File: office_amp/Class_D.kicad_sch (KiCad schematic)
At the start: 40 parts, among them J3 Conn_01x02_Female, J4 Conn_01x02_Female, J5 Conn_01x02_Female, J6 Conn_01x02_Female, J7 Screw_Terminal_01x04, U6 TPA3123D2

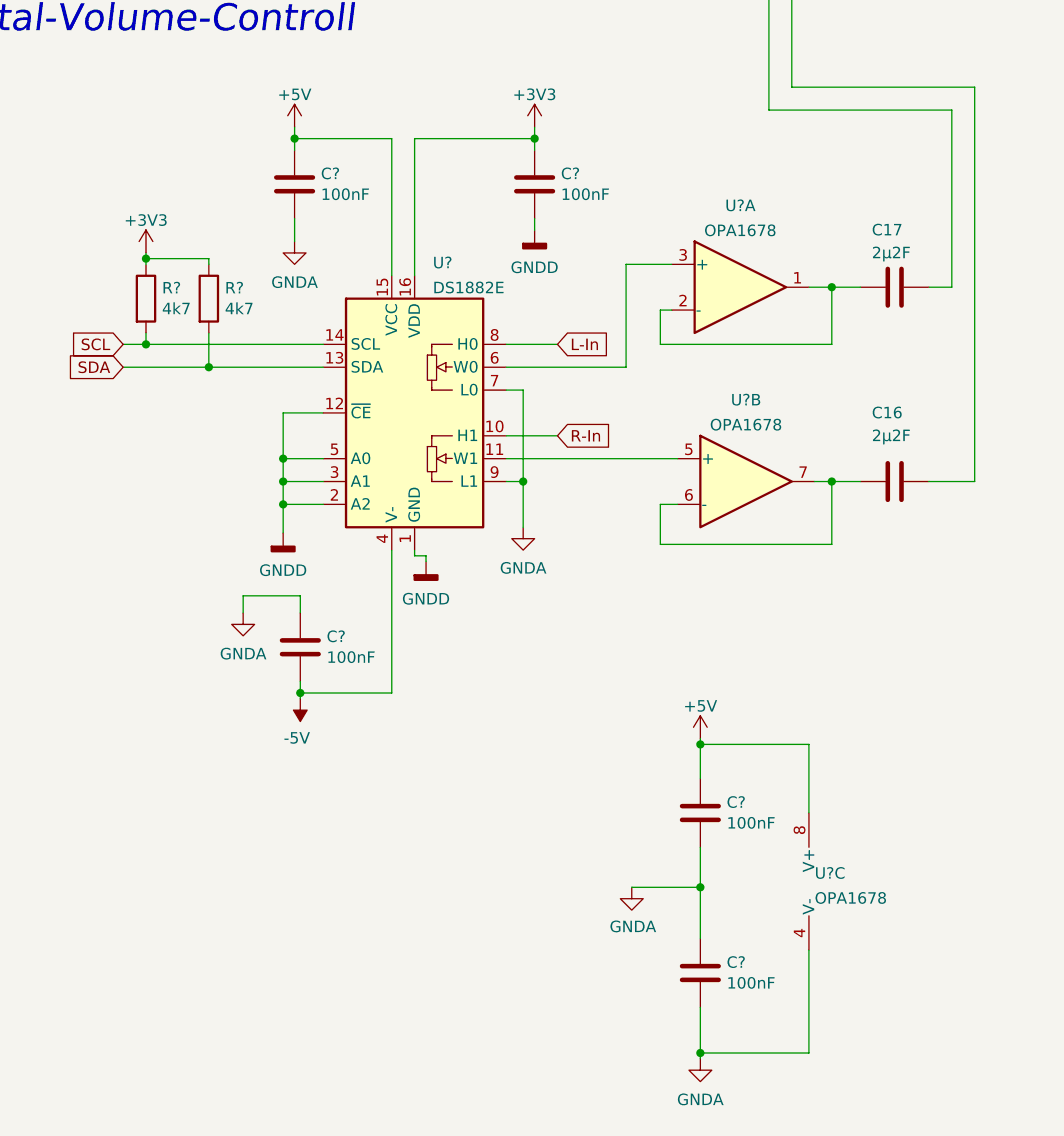
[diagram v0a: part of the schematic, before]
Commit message: Changed Components to available parts
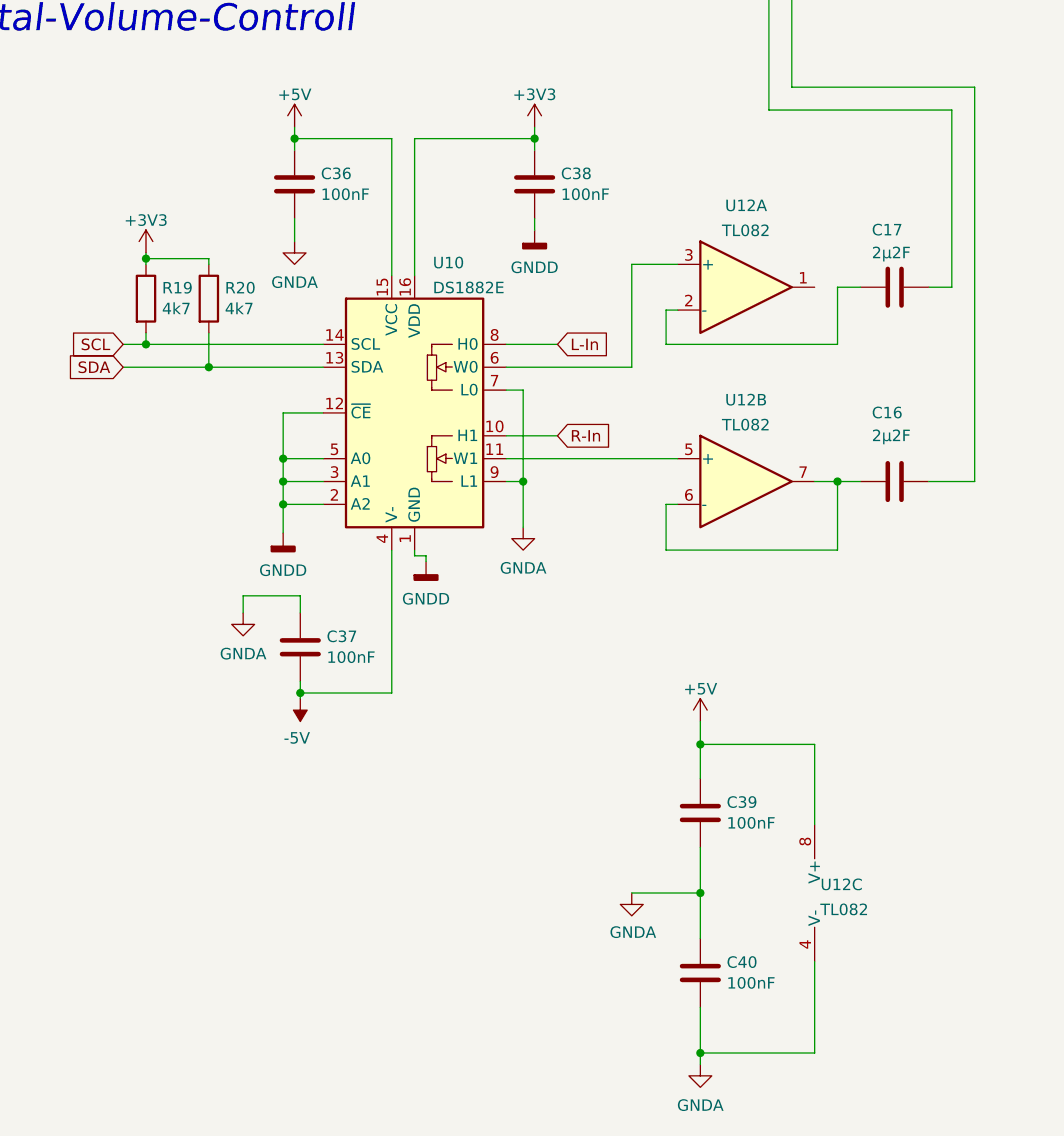
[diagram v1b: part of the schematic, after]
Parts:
- removed U? (x3): OPA1678, symbol Amplifier_Operational:OPA1678
- added U12: TL082, Package_SO:SO-8_3.9x4.9mm_P1.27mm, symbol Amplifier_Operational:TL082
- C10, C11, C24, C25: footprint Capacitor_THT:CP_Radial_D12.5mm_P5.00mm -> Capacitor_THT:CP_Radial_D10.0mm_P5.00mm
- C22, C23: footprint Capacitor_SMD:C_0805_2012Metric_Pad1.18x1.45mm_HandSolder -> Capacitor_THT:C_Rect_L7.2mm_W4.5mm_P5.00mm_FKS2_FKP2_MKS2_MKP2
- L1, L2: footprint Inductor_SMD:L_Fastron_PISN_Handsoldering -> office_amp:L_Bourns-PM5022
- gave numbers to parts that had none: 8
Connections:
- net +5V: now also U12.8 (V+)
- net GNDA: now also U12.4 (V-)
- net at C16.2: now also U12.6 (-), U12.7
- net at C17.2: now also U12.2 (-)
- net at U10.11 (W1): now also U12.5 (+)
- net at U10.6 (W0): now also U12.3 (+)

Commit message: First positioning of new components (top site), added mounting holes for case  compabillity (Donau 523178)
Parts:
- removed J3, J4, J5, J6: Conn_01x02_Female, Connector_PinHeader_2.54mm:PinHeader_1x02_P2.54mm_Vertical, symbol Connector:Conn_01x02_Female
- added Q6, Q8, Q9: BC856, Package_TO_SOT_SMD:SOT-23, symbol Transistor_BJT:BC856
- added Q7: BC850, Package_TO_SOT_SMD:SOT-23, symbol Transistor_BJT:BC850
- added R21, R22, R23, R24, R25, R26, R27, R28: 10k, Resistor_SMD:R_0805_2012Metric_Pad1.20x1.40mm_HandSolder, symbol Device:R
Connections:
- net +3V3: now also R4.1, Q6.2 (E), Q8.2 (E), Q9.2 (E), R23.2, R27.2, R28.2
- net -5V: now also C40.2, U12.4 (V-)
- net GAIN0: now also R2.1, Q6.3 (C); no longer R2.2
- net GAIN1: now also R1.1, Q9.3 (C); no longer R1.2
- net GNDA: no longer C40.2, U12.4 (V-)
- net GNDREF: now also R1.2, R2.2, R3.2, Q7.2 (E), R24.1; no longer R4.2
- net MUTE: now also R4.2, Q7.3 (C); no longer R4.1
- net V+: no longer R1.1, R2.1, R3.1
- net ~{SD}: now also R3.1, Q8.3 (C); no longer R3.2
- net at C17.2, U12.2 (-): now also U12.1
- new net: Q9.1 (B), R26.2, R28.1
- new net: Q7.1 (B), R22.2, R24.2
- new net: Q6.1 (B), R21.2, R23.1
- new net: Q8.1 (B), R25.2, R27.1
- new net AMP-GAIN0: R21.1
- new net AMP-GAIN1: R26.1
- new net AMP-ShutDown: R25.1
- new net ~{AMP-Mute}: R22.1
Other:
- note removed: "Gain"
- note removed: "J3 -> set to shut down the amplifier J4,J5 -> set to set the gain J6 -> set to mute the amplifier"
- note removed: "Jumper Configuration"
- note removed: "Mute"
- note removed: "Shutdown"
- moved on the sheet: C10, C11, C12, C13, C14, C15, C18, C19, C20, C21, C22, C23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

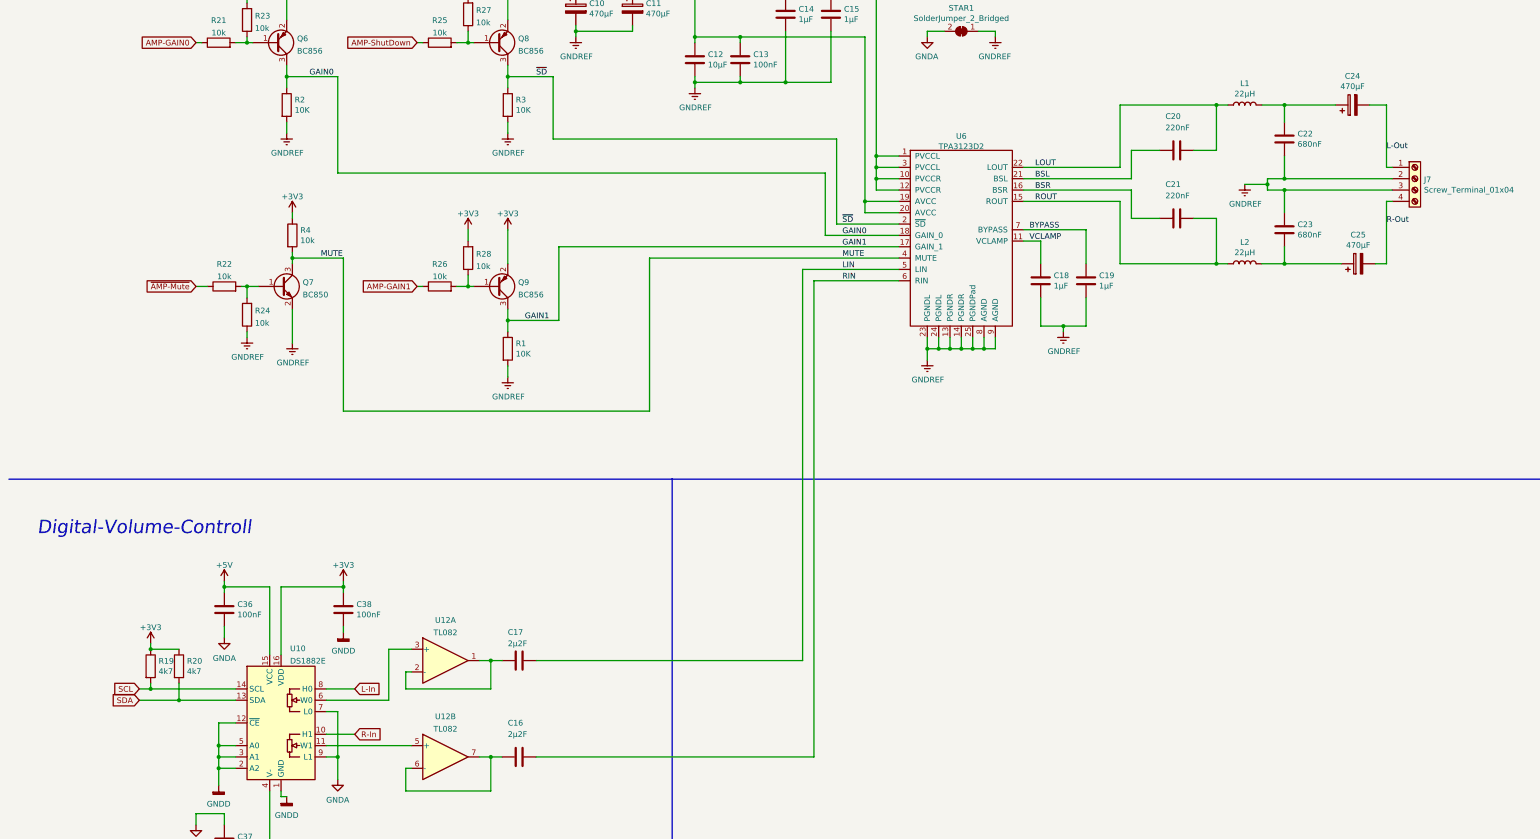
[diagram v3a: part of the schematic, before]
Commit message: added testpoints, corrected footprints, removed ground loop dgnd gnda
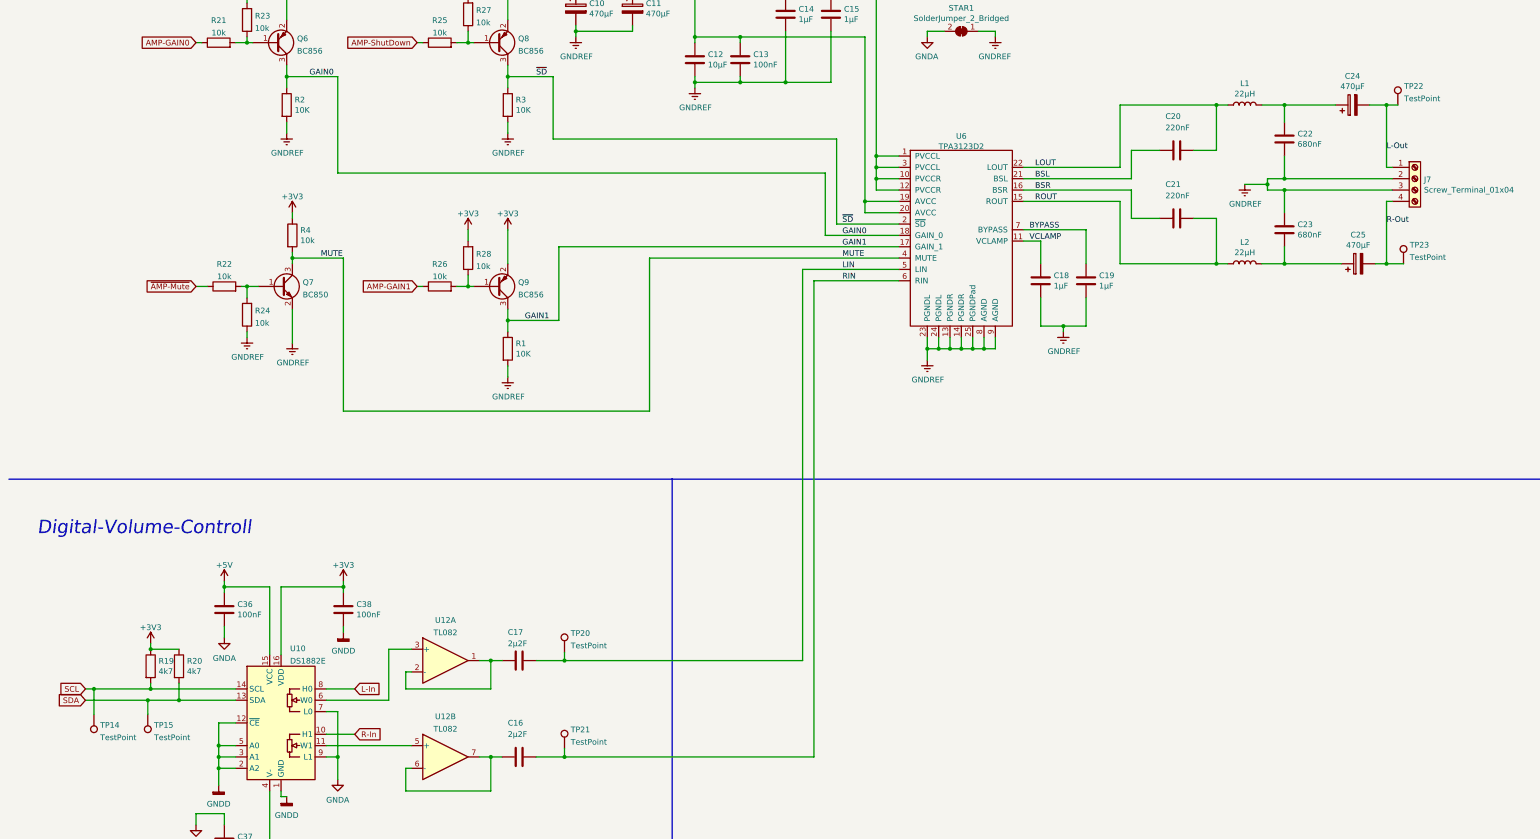
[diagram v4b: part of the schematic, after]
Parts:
- added TP14, TP15, TP20, TP21, TP22, TP23: TestPoint, TestPoint:TestPoint_Pad_D1.0mm, symbol Connector:TestPoint
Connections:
- net L-Out: now also TP22.1
- net LIN: now also TP20.1
- net R-Out: now also TP23.1
- net RIN: now also TP21.1
- net SCL: now also TP14.1
- net SDA: now also TP15.1
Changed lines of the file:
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@@
   (junction (at 59.69 201.93) (diameter 0) (color 0 0 0 0)
   )
+  (junction (at 321.31 91.44) (diameter 0) (color 0 0 0 0)
+  )
   (junction (at 204.47 77.47) (diameter 0) (color 0 0 0 0)
   )
@@
   (junction (at 226.06 110.49) (diameter 0) (color 0 0 0 0)
   )
+  (junction (at 321.31 55.88) (diameter 0) (color 0 0 0 0)
+  )
   (junction (at 120.65 201.93) (diameter 0) (color 0 0 0 0)
   )
@@
   (junction (at 105.41 265.43) (diameter 0) (color 0 0 0 0)
   )
+  (junction (at 43.815 189.23) (diameter 0) (color 0 0 0 0)
+  )
   (junction (at 298.45 72.39) (diameter 0) (color 0 0 0 0)
   )
@@
   (junction (at 196.85 29.21) (diameter 0) (color 0 0 0 0)
   )
+  (junction (at 137.16 180.34) (diameter 0) (color 0 0 0 0)
+  )
   (junction (at 60.96 163.83) (diameter 0) (color 0 0 0 0)
   )
+  (junction (at 137.16 201.93) (diameter 0) (color 0 0 0 0)
+  )
   (junction (at 166.37 29.21) (diameter 0) (color 0 0 0 0)
   )
@@
   (junction (at 115.57 96.52) (diameter 0) (color 0 0 0 0)
   )
+  (junction (at 31.75 186.69) (diameter 0) (color 0 0 0 0)
+  )
   (junction (at 59.69 204.47) (diameter 0) (color 0 0 0 0)
   )
@@
     (stroke (width 0) (type default) (color 0 0 0 0))
   )
-  (wire (pts (xy 41.91 186.69) (xy 44.45 186.69))
+  (wire (pts (xy 29.845 186.69) (xy 31.75 186.69))
     (stroke (width 0) (type default) (color 0 0 0 0))
   )
@@
     (stroke (width 0) (type default) (color 0 0 0 0))
   )
-  (wire (pts (xy 41.91 189.23) (xy 50.8 189.23))
+  (wire (pts (xy 29.845 189.23) (xy 43.815 189.23))
     (stroke (width 0) (type default) (color 0 0 0 0))
   )
@@
     (stroke (width 0) (type default) (color 0 0 0 0))
   )
+  (wire (pts (xy 31.75 192.405) (xy 31.75 186.69))
+    (stroke (width 0) (type default) (color 0 0 0 0))
+  )
   (wire (pts (xy 105.41 260.35) (xy 105.41 265.43))
     (stroke (width 0) (type default) (color 0 0 0 0))
@@
     (stroke (width 0) (type default) (color 0 0 0 0))
   )
+  (wire (pts (xy 137.16 200.025) (xy 137.16 201.93))
+    (stroke (width 0) (type default) (color 0 0 0 0))
+  )
   (wire (pts (xy 240.03 86.36) (xy 243.84 86.36))
     (stroke (width 0) (type default) (color 0 0 0 0))
@@
     (stroke (width 0) (type default) (color 0 0 0 0))
   )
+  (wire (pts (xy 43.815 189.23) (xy 43.815 192.405))
+    (stroke (width 0) (type default) (color 0 0 0 0))
+  )
+  (wire (pts (xy 137.16 178.435) (xy 137.16 180.34))
+    (stroke (width 0) (type default) (color 0 0 0 0))
+  )
   (wire (pts (xy 240.03 72.39) (xy 264.16 72.39))
     (stroke (width 0) (type default) (color 0 0 0 0))
@@
     (stroke (width 0) (type default) (color 0 0 0 0))
   )
+  (wire (pts (xy 31.75 186.69) (xy 44.45 186.69))
+    (stroke (width 0) (type default) (color 0 0 0 0))
+  )
+  (wire (pts (xy 137.16 180.34) (xy 190.5 180.34))
+    (stroke (width 0) (type default) (color 0 0 0 0))
+  )
   (wire (pts (xy 87.63 90.17) (xy 87.63 124.46))
     (stroke (width 0) (type default) (color 0 0 0 0))
@@
     (stroke (width 0) (type default) (color 0 0 0 0))
   )
+  (wire (pts (xy 321.31 91.44) (xy 325.12 91.44))
+    (stroke (width 0) (type default) (color 0 0 0 0))
+  )
   (wire (pts (xy 283.21 66.04) (xy 283.21 55.88))
     (stroke (width 0) (type default) (color 0 0 0 0))
@@
     (stroke (width 0) (type default) (color 0 0 0 0))
   )
-  (wire (pts (xy 130.81 180.34) (xy 190.5 180.34))
+  (wire (pts (xy 130.81 180.34) (xy 137.16 180.34))
+    (stroke (width 0) (type default) (color 0 0 0 0))
+  )
+  (wire (pts (xy 321.31 55.88) (xy 323.85 55.88))
+    (stroke (width 0) (type default) (color 0 0 0 0))
+  )
+  (wire (pts (xy 43.815 189.23) (xy 50.8 189.23))
     (stroke (width 0) (type default) (color 0 0 0 0))
   )
@@
     (stroke (width 0) (type default) (color 0 0 0 0))
   )
+  (wire (pts (xy 137.16 201.93) (xy 193.04 201.93))
+    (stroke (width 0) (type default) (color 0 0 0 0))
+  )
   (wire (pts (xy 105.41 228.6) (xy 105.41 231.14))
     (stroke (width 0) (type default) (color 0 0 0 0))
@@
     (stroke (width 0) (type default) (color 0 0 0 0))
   )
-  (wire (pts (xy 130.81 201.93) (xy 193.04 201.93))
+  (wire (pts (xy 130.81 201.93) (xy 137.16 201.93))
     (stroke (width 0) (type default) (color 0 0 0 0))
   )
@@
     )
   )
-  (global_label "SDA" (shape input) (at 41.91 189.23 180) (fields_autoplaced)
+  (global_label "SDA" (shape input) (at 29.845 189.23 180) (fields_autoplaced)
     (effects (font (size 1.27 1.27)) (justify right))
-    (property "Intersheet References" "${INTERSHEET_REFS}" (id 0) (at 36.0177 189.1506 0)
+    (property "Intersheet References" "${INTERSHEET_REFS}" (id 0) (at 23.9527 189.1506 0)
       (effects (font (size 1.27 1.27)) (justify right) hide)
     )
@@
     )
   )
-  (global_label "SCL" (shape input) (at 41.91 186.69 180) (fields_autoplaced)
+  (global_label "SCL" (shape input) (at 29.845 186.69 180) (fields_autoplaced)
     (effects (font (size 1.27 1.27)) (justify right))
-    (property "Intersheet References" "${INTERSHEET_REFS}" (id 0) (at 36.0782 186.6106 0)
+    (property "Intersheet References" "${INTERSHEET_REFS}" (id 0) (at 24.0132 186.6106 0)
       (effects (font (size 1.27 1.27)) (justify right) hide)
     )
@@
     (pin "2")
   )
+  (symbol (lib_id "Connector:TestPoint") (at 43.815 192.405 180) (unit 1)
+    (in_bom yes) (on_board yes) (fields_autoplaced)
+    (property "Reference" "TP15" (id 0) (at 45.212 194.7985 0)
+      (effects (font (size 1.27 1.27)) (justify right))
+    )
+    (property "Value" "TestPoint" (id 1) (at 45.212 197.5736 0)
+      (effects (font (size 1.27 1.27)) (justify right))
+    )
+    (property "Footprint" "TestPoint:TestPoint_Pad_D1.0mm" (id 2) (at 38.735 192.405 0)
+      (effects (font (size 1.27 1.27)) hide)
+    )
+    (property "Datasheet" "~" (id 3) (at 38.735 192.405 0)
+      (effects (font (size 1.27 1.27)) hide)
+    )
+    (pin "1")
+  )
   (symbol (lib_id "power:+3V3") (at 115.57 30.48 0) (unit 1)
     (in_bom yes) (on_board yes) (fields_autoplaced)
@@
     (pin "1")
   )
+  (symbol (lib_id "Connector:TestPoint") (at 137.16 178.435 0) (unit 1)
+    (in_bom yes) (on_board yes) (fields_autoplaced)
+    (property "Reference" "TP20" (id 0) (at 138.557 174.2245 0)
+      (effects (font (size 1.27 1.27)) (justify left))
+    )
+    (property "Value" "TestPoint" (id 1) (at 138.557 176.9996 0)
+      (effects (font (size 1.27 1.27)) (justify left))
+    )
+    (property "Footprint" "TestPoint:TestPoint_Pad_D1.0mm" (id 2) (at 142.24 178.435 0)
+      (effects (font (size 1.27 1.27)) hide)
+    )
+    (property "Datasheet" "~" (id 3) (at 142.24 178.435 0)
+      (effects (font (size 1.27 1.27)) hide)
+    )
+    (pin "1")
+  )
   (symbol (lib_id "Device:R") (at 109.22 41.91 90) (unit 1)
     (in_bom yes) (on_board yes) (fields_autoplaced)
@@
     (pin "2")
   )
+  (symbol (lib_id "Connector:TestPoint") (at 137.16 200.025 0) (unit 1)
+    (in_bom yes) (on_board yes) (fields_autoplaced)
+    (property "Reference" "TP21" (id 0) (at 138.557 195.8145 0)
+      (effects (font (size 1.27 1.27)) (justify left))
+    )
+    (property "Value" "TestPoint" (id 1) (at 138.557 198.5896 0)
+      (effects (font (size 1.27 1.27)) (justify left))
+    )
+    (property "Footprint" "TestPoint:TestPoint_Pad_D1.0mm" (id 2) (at 142.24 200.025 0)
+      (effects (font (size 1.27 1.27)) hide)
+    )
+    (property "Datasheet" "~" (id 3) (at 142.24 200.025 0)
+      (effects (font (size 1.27 1.27)) hide)
+    )
+    (pin "1")
+  )
   (symbol (lib_id "power:GNDA") (at 86.36 207.01 0) (unit 1)
     (in_bom yes) (on_board yes) (fields_autoplaced)
@@
     )
     (property "Datasheet" "" (id 3) (at 115.57 83.82 0)
+      (effects (font (size 1.27 1.27)) hide)
+    )
+    (pin "1")
+  )
+  (symbol (lib_id "Connector:TestPoint") (at 323.85 55.88 0) (unit 1)
+    (in_bom yes) (on_board yes) (fields_autoplaced)
+    (property "Reference" "TP22" (id 0) (at 325.247 51.6695 0)
+      (effects (font (size 1.27 1.27)) (justify left))
+    )
+    (property "Value" "TestPoint" (id 1) (at 325.247 54.4446 0)
+      (effects (font (size 1.27 1.27)) (justify left))
+    )
+    (property "Footprint" "TestPoint:TestPoint_Pad_D1.0mm" (id 2) (at 328.93 55.88 0)
+      (effects (font (size 1.27 1.27)) hide)
+    )
+    (property "Datasheet" "~" (id 3) (at 328.93 55.88 0)
       (effects (font (size 1.27 1.27)) hide)
     )
@@
     (pin "2")
   )
+  (symbol (lib_id "Connector:TestPoint") (at 325.12 91.44 0) (unit 1)
+    (in_bom yes) (on_board yes) (fields_autoplaced)
+    (property "Reference" "TP23" (id 0) (at 326.517 87.2295 0)
+      (effects (font (size 1.27 1.27)) (justify left))
+    )
+    (property "Value" "TestPoint" (id 1) (at 326.517 90.0046 0)
+      (effects (font (size 1.27 1.27)) (justify left))
+    )
+    (property "Footprint" "TestPoint:TestPoint_Pad_D1.0mm" (id 2) (at 330.2 91.44 0)
+      (effects (font (size 1.27 1.27)) hide)
+    )
+    (property "Datasheet" "~" (id 3) (at 330.2 91.44 0)
+      (effects (font (size 1.27 1.27)) hide)
+    )
+    (pin "1")
+  )
   (symbol (lib_id "power:GNDD") (at 74.93 210.82 0) (unit 1)
     (in_bom yes) (on_board yes) (fields_autoplaced)
@@
       (effects (font (size 1.27 1.27)) hide)
     )
+    (pin "1")
+  )
+  (symbol (lib_id "Connector:TestPoint") (at 31.75 192.405 180) (unit 1)
+    (in_bom yes) (on_board yes) (fields_autoplaced)
+    (property "Reference" "TP14" (id 0) (at 33.147 194.7985 0)
+      (effects (font (size 1.27 1.27)) (justify right))
+    )
+    (property "Value" "TestPoint" (id 1) (at 33.147 197.5736 0)
+      (effects (font (size 1.27 1.27)) (justify right))
+    )
+    (property "Footprint" "TestPoint:TestPoint_Pad_D1.0mm" (id 2) (at 26.67 192.405 0)
+      (effects (font (size 1.27 1.27)) hide)
+    )
+    (property "Datasheet" "~" (id 3) (at 26.67 192.405 0)
+      (effects (font (size 1.27 1.27)) hide)
+    )
